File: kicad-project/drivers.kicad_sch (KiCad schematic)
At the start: 11 parts

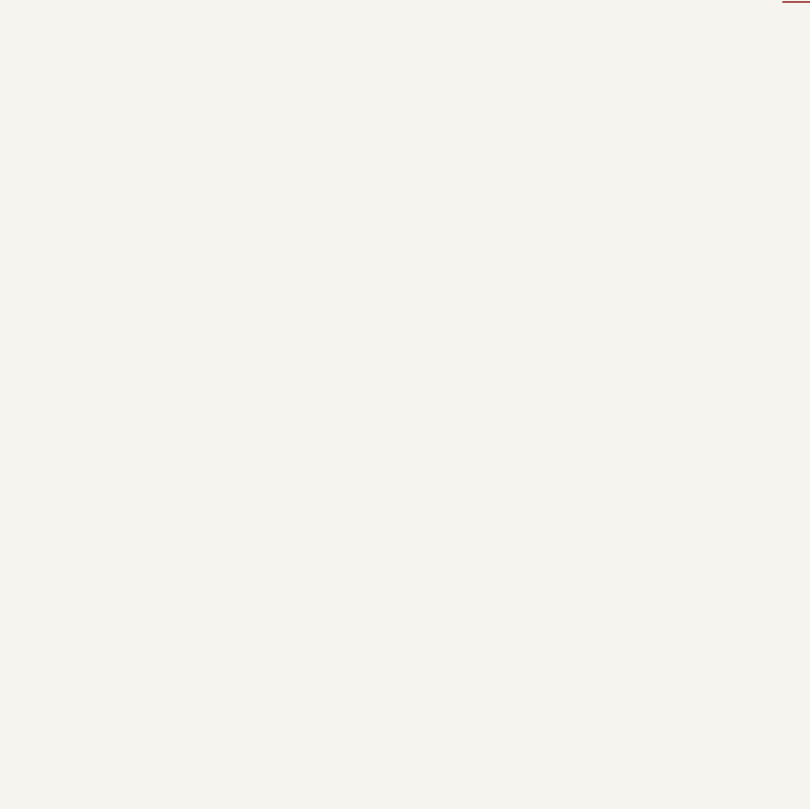
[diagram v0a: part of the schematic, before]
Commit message: hw: rename poject and create project library
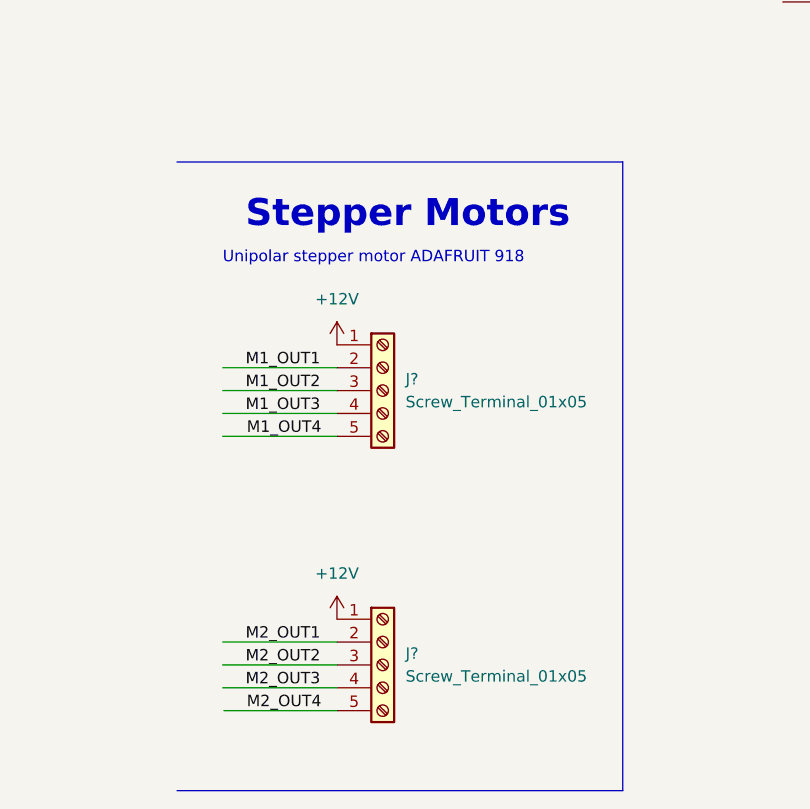
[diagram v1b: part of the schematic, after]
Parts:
- added J? (x2): Screw_Terminal_01x05, TerminalBlock_TE-Connectivity:TerminalBlock_TE_282834-5_1x05_P2.54mm_Horizontal, symbol Connector:Screw_Terminal_01x05
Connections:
- net +12V: now also J?.1 (Pin_1), J?.1 (Pin_1)
- new net M1_OUT1: J?.2 (Pin_2)
- new net M1_OUT2: J?.3 (Pin_3)
- new net M1_OUT3: J?.4 (Pin_4)
- new net M1_OUT4: J?.5 (Pin_5)
- new net M2_OUT1: J?.2 (Pin_2)
- new net M2_OUT2: J?.3 (Pin_3)
- new net M2_OUT3: J?.4 (Pin_4)
- new net M2_OUT4: J?.5 (Pin_5)
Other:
- note added: "Stepper Motors"
- note added: "Unipolar stepper motor ADAFRUIT 918"
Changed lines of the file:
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@@
+    (stroke (width 0) (type default) (color 0 0 0 0))
+  )
+  (wire (pts (xy 128.27 154.94) (xy 140.97 154.94))
     (stroke (width 0) (type default) (color 0 0 0 0))
   )
@@
     (stroke (width 0) (type default) (color 0 0 0 0))
   )
+  (wire (pts (xy 128.3981 185.42) (xy 140.97 185.42))
+    (stroke (width 0) (type default) (color 0 0 0 0))
+  )
   (wire (pts (xy 36.83 64.77) (xy 58.42 64.77))
     (stroke (width 0) (type default) (color 0 0 0 0))
@@
     (stroke (width 0) (type default) (color 0 0 0 0))
   )
+  (wire (pts (xy 128.27 177.8) (xy 140.97 177.8))
+    (stroke (width 0) (type default) (color 0 0 0 0))
+  )
+  (wire (pts (xy 128.27 149.86) (xy 140.97 149.86))
+    (stroke (width 0) (type default) (color 0 0 0 0))
+  )
   (wire (pts (xy 88.9 87.63) (xy 96.52 87.63))
     (stroke (width 0) (type default) (color 0 0 0 0))
@@
     (stroke (width 0) (type default) (color 0 0 0 0))
   )
+  (polyline (pts (xy 123.19 124.46) (xy 172.72 124.46))
+    (stroke (width 0) (type default) (color 0 0 0 0))
+  )
   (wire (pts (xy 110.49 50.8) (xy 123.19 50.8))
     (stroke (width 0) (type default) (color 0 0 0 0))
   )
+  (polyline (pts (xy 172.72 194.31) (xy 172.72 124.46))
+    (stroke (width 0) (type default) (color 0 0 0 0))
+  )
   (wire (pts (xy 97.79 30.48) (xy 109.22 30.48))
     (stroke (width 0) (type default) (color 0 0 0 0))
   )
+  (wire (pts (xy 128.27 180.34) (xy 140.97 180.34))
+    (stroke (width 0) (type default) (color 0 0 0 0))
+  )
   (wire (pts (xy 88.9 85.09) (xy 107.95 85.09))
     (stroke (width 0) (type default) (color 0 0 0 0))
@@
     (stroke (width 0) (type default) (color 0 0 0 0))
   )
+  (wire (pts (xy 128.27 147.32) (xy 140.97 147.32))
+    (stroke (width 0) (type default) (color 0 0 0 0))
+  )
+  (wire (pts (xy 128.27 182.88) (xy 140.97 182.88))
+    (stroke (width 0) (type default) (color 0 0 0 0))
+  )
   (wire (pts (xy 88.9 50.8) (xy 88.9 52.07))
     (stroke (width 0) (type default) (color 0 0 0 0))
@@
     (stroke (width 0) (type default) (color 0 0 0 0))
   )
+  (polyline (pts (xy 123.19 194.31) (xy 172.72 194.31))
+    (stroke (width 0) (type default) (color 0 0 0 0))
+  )
+  (wire (pts (xy 128.27 152.4) (xy 140.97 152.4))
+    (stroke (width 0) (type default) (color 0 0 0 0))
+  )
   (wire (pts (xy 97.79 59.69) (xy 97.79 60.96))
     (stroke (width 0) (type default) (color 0 0 0 0))
@@
     (stroke (width 0) (type default) (color 0 0 0 0))
   )
+  (text "Unipolar stepper motor ADAFRUIT 918" (at 128.27 135.89 0)
+    (effects (font (size 1.27 1.27)) (justify left bottom))
+  )
+  (text "Stepper Motors\n" (at 130.81 132.08 0)
+    (effects (font (size 3 3) (thickness 0.6) bold) (justify left bottom))
+  )
   (label "VBB" (at 91.44 50.8 0)
     (effects (font (size 1.27 1.27)) (justify left bottom))
   )
+  (label "M1_OUT3" (at 130.81 152.4 0)
+    (effects (font (size 1.27 1.27)) (justify left bottom))
+  )
   (label "VCP" (at 100.33 60.96 0)
+    (effects (font (size 1.27 1.27)) (justify left bottom))
+  )
+  (label "M2_OUT1" (at 130.81 177.8 0)
+    (effects (font (size 1.27 1.27)) (justify left bottom))
+  )
+  (label "M2_OUT3" (at 130.81 182.88 0)
+    (effects (font (size 1.27 1.27)) (justify left bottom))
+  )
+  (label "M2_OUT4" (at 130.9381 185.42 0)
     (effects (font (size 1.27 1.27)) (justify left bottom))
   )
@@
     (effects (font (size 1.27 1.27)) (justify left bottom))
   )
+  (label "M1_OUT4" (at 130.9381 154.94 0)
+    (effects (font (size 1.27 1.27)) (justify left bottom))
+  )
+  (label "M1_OUT2" (at 130.81 149.86 0)
+    (effects (font (size 1.27 1.27)) (justify left bottom))
+  )
   (label "SLEEP" (at 54.61 67.31 180)
     (effects (font (size 1.27 1.27)) (justify right bottom))
+  )
+  (label "M2_OUT2" (at 130.81 180.34 0)
+    (effects (font (size 1.27 1.27)) (justify left bottom))
+  )
+  (label "M1_OUT1" (at 130.81 147.32 0)
+    (effects (font (size 1.27 1.27)) (justify left bottom))
   )
   (symbol (lib_name "A4988SETTR-T_1") (lib_id "A4988:A4988SETTR-T") (at 210.82 81.28 0) (unit 1)
@@
     (pin "9")
   )
+  (symbol (lib_id "power:+12V") (at 140.97 175.26 0) (unit 1)
+    (in_bom yes) (on_board yes) (fields_autoplaced)
+    (property "Reference" "#PWR?" (id 0) (at 140.97 179.07 0)
+      (effects (font (size 1.27 1.27)) hide)
+    )
+    (property "Value" "+12V" (id 1) (at 140.97 170.18 0))
+    (property "Footprint" "" (id 2) (at 140.97 175.26 0)
+      (effects (font (size 1.27 1.27)) hide)
+    )
+    (property "Datasheet" "" (id 3) (at 140.97 175.26 0)
+      (effects (font (size 1.27 1.27)) hide)
+    )
+    (pin "1")
+  )
   (symbol (lib_id "power:GND") (at 107.95 92.71 0) (unit 1)
     (in_bom yes) (on_board yes) (fields_autoplaced)
@@
     (pin "9")
   )
+  (symbol (lib_id "Connector:Screw_Terminal_01x05") (at 146.05 180.34 0) (unit 1)
+    (in_bom yes) (on_board yes) (fields_autoplaced)
+    (property "Reference" "J?" (id 0) (at 148.59 179.0699 0)
+      (effects (font (size 1.27 1.27)) (justify left))
+    )
+    (property "Value" "Screw_Terminal_01x05" (id 1) (at 148.59 181.6099 0)
+      (effects (font (size 1.27 1.27)) (justify left))
+    )
+    (property "Footprint" "TerminalBlock_TE-Connectivity:TerminalBlock_TE_282834-5_1x05_P2.54mm_Horizontal" (id 2) (at 146.05 180.34 0)
+      (effects (font (size 1.27 1.27)) hide)
+    )
+    (property "Datasheet" "~" (id 3) (at 146.05 180.34 0)
+      (effects (font (size 1.27 1.27)) hide)
+    )
+    (pin "1")
+    (pin "2")
+    (pin "3")
+    (pin "4")
+    (pin "5")
+  )
   (symbol (lib_id "Device:C") (at 97.79 38.1 0) (unit 1)
     (in_bom yes) (on_board yes) (fields_autoplaced)
@@
     (pin "2")
   )
+  (symbol (lib_id "power:+12V") (at 140.97 144.78 0) (unit 1)
+    (in_bom yes) (on_board yes) (fields_autoplaced)
+    (property "Reference" "#PWR?" (id 0) (at 140.97 148.59 0)
+      (effects (font (size 1.27 1.27)) hide)
+    )
+    (property "Value" "+12V" (id 1) (at 140.97 139.7 0))
+    (property "Footprint" "" (id 2) (at 140.97 144.78 0)
+      (effects (font (size 1.27 1.27)) hide)
+    )
+    (property "Datasheet" "" (id 3) (at 140.97 144.78 0)
+      (effects (font (size 1.27 1.27)) hide)
+    )
+    (pin "1")
+  )
+  (symbol (lib_id "Connector:Screw_Terminal_01x05") (at 146.05 149.86 0) (unit 1)
+    (in_bom yes) (on_board yes) (fields_autoplaced)
+    (property "Reference" "J?" (id 0) (at 148.59 148.5899 0)
+      (effects (font (size 1.27 1.27)) (justify left))
+    )
+    (property "Value" "Screw_Terminal_01x05" (id 1) (at 148.59 151.1299 0)
+      (effects (font (size 1.27 1.27)) (justify left))
+    )
+    (property "Footprint" "TerminalBlock_TE-Connectivity:TerminalBlock_TE_282834-5_1x05_P2.54mm_Horizontal" (id 2) (at 146.05 149.86 0)
+      (effects (font (size 1.27 1.27)) hide)
+    )
+    (property "Datasheet" "~" (id 3) (at 146.05 149.86 0)
+      (effects (font (size 1.27 1.27)) hide)
+    )
+    (pin "1")
+    (pin "2")
+    (pin "3")
+    (pin "4")
+    (pin "5")
+  )
   (symbol (lib_id "power:GND") (at 88.9 102.87 0) (unit 1)

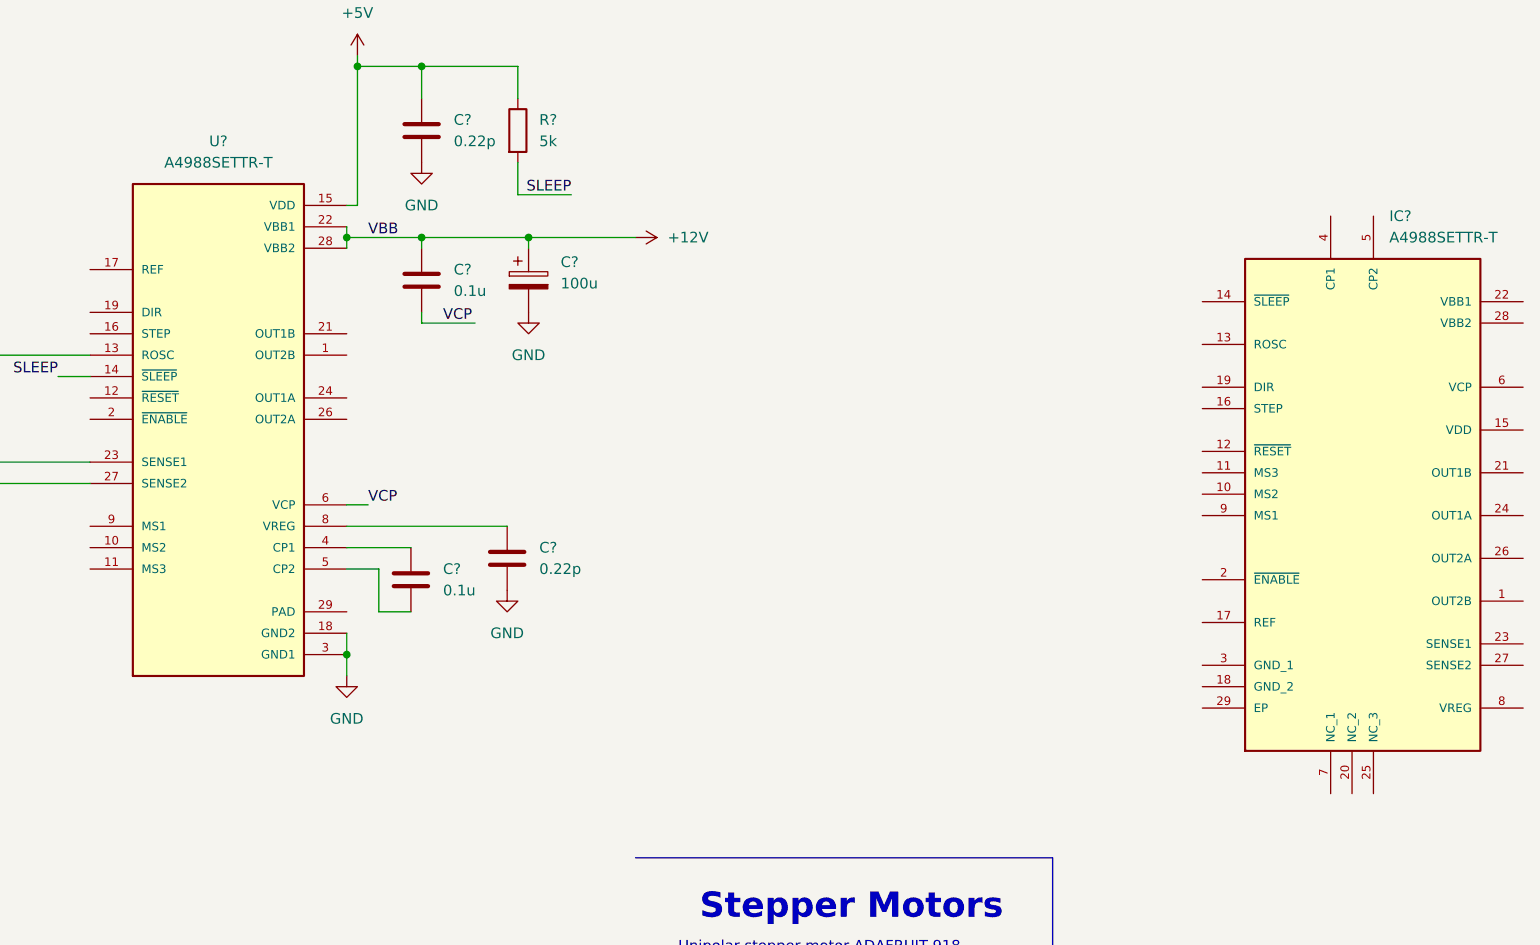
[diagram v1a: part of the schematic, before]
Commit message: hw: add power managment
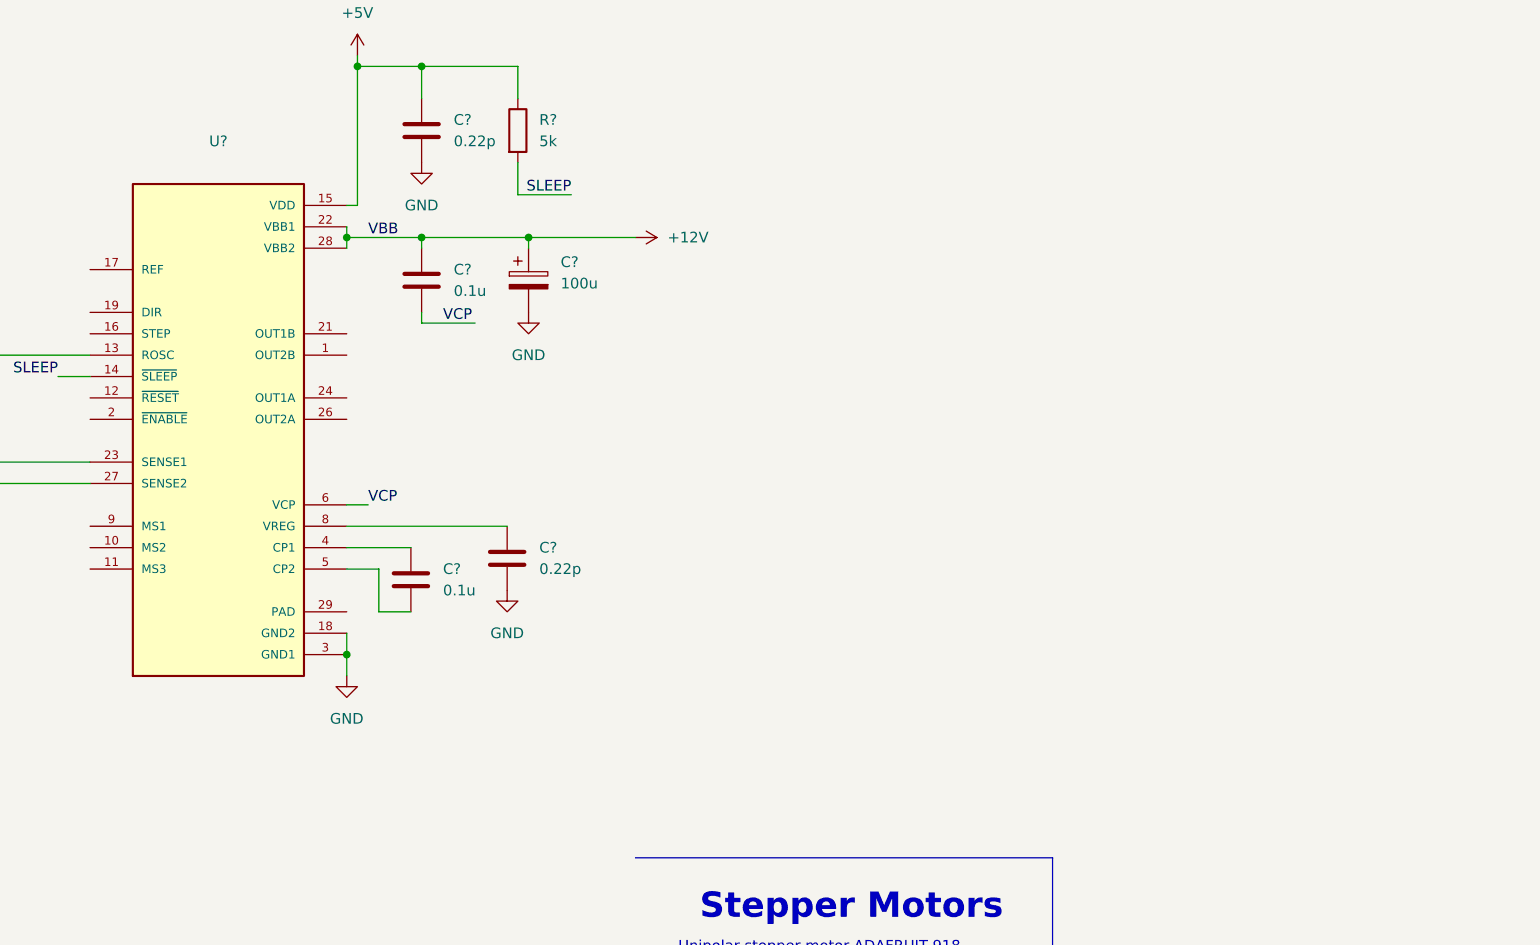
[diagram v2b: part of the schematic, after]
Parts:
- removed IC?: A4988SETTR-T, QFN50P500X500X100-29N, symbol A4988:A4988SETTR-T
- U?: value A4988SETTR-T -> (none); footprint QFN50P500X500X90-29N -> (none)
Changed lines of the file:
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@@
     (effects (font (size 1.27 1.27)) (justify left bottom))
-  )
-  (symbol (lib_name "A4988SETTR-T_1") (lib_id "A4988:A4988SETTR-T") (at 210.82 81.28 0) (unit 1)
-    (in_bom yes) (on_board yes) (fields_autoplaced)
-    (property "Reference" "IC?" (id 0) (at 212.6997 48.26 0)
-      (effects (font (size 1.27 1.27)) (justify left))
-    )
-    (property "Value" "A4988SETTR-T" (id 1) (at 212.6997 50.8 0)
-      (effects (font (size 1.27 1.27)) (justify left))
-    )
-    (property "Footprint" "QFN50P500X500X100-29N" (id 2) (at 210.82 81.28 0)
-      (effects (font (size 1.27 1.27)) (justify left bottom) hide)
-    )
-    (property "Datasheet" "" (id 3) (at 210.82 81.28 0)
-      (effects (font (size 1.27 1.27)) (justify left bottom) hide)
-    )
-    (property "RS_PART_NUMBER" "" (id 4) (at 210.82 81.28 0)
-      (effects (font (size 1.27 1.27)) (justify left bottom) hide)
-    )
-    (property "MOUSER_PRICE-STOCK" "" (id 5) (at 210.82 81.28 0)
-      (effects (font (size 1.27 1.27)) (justify left bottom) hide)
-    )
-    (property "MANUFACTURER_PART_NUMBER" "A4988SETTR-T" (id 6) (at 210.82 81.28 0)
-      (effects (font (size 1.27 1.27)) (justify left bottom) hide)
-    )
-    (property "MOUSER_PART_NUMBER" "" (id 7) (at 210.82 81.28 0)
-      (effects (font (size 1.27 1.27)) (justify left bottom) hide)
-    )
-    (property "DESCRIPTION" "DMOS Microstepping Driver with Translator  and Overcurrent Protection" (id 8) (at 210.82 81.28 0)
-      (effects (font (size 1.27 1.27)) (justify left bottom) hide)
-    )
-    (property "RS_PRICE-STOCK" "" (id 9) (at 210.82 81.28 0)
-      (effects (font (size 1.27 1.27)) (justify left bottom) hide)
-    )
-    (property "MANUFACTURER_NAME" "Allegro Microsystems" (id 10) (at 210.82 81.28 0)
-      (effects (font (size 1.27 1.27)) (justify left bottom) hide)
-    )
-    (property "HEIGHT" "1mm" (id 11) (at 210.82 81.28 0)
-      (effects (font (size 1.27 1.27)) (justify left bottom) hide)
-    )
-    (pin "1")
-    (pin "10")
-    (pin "11")
-    (pin "12")
-    (pin "13")
-    (pin "14")
-    (pin "15")
-    (pin "16")
-    (pin "17")
-    (pin "18")
-    (pin "19")
-    (pin "2")
-    (pin "20")
-    (pin "21")
-    (pin "22")
-    (pin "23")
-    (pin "24")
-    (pin "25")
-    (pin "26")
-    (pin "27")
-    (pin "28")
-    (pin "29")
-    (pin "3")
-    (pin "4")
-    (pin "5")
-    (pin "6")
-    (pin "7")
-    (pin "8")
-    (pin "9")
   )
   (symbol (lib_id "power:+12V") (at 140.97 175.26 0) (unit 1)
@@
     (in_bom yes) (on_board yes) (fields_autoplaced)
     (property "Reference" "U?" (id 0) (at 73.66 39.37 0))
-    (property "Value" "A4988SETTR-T" (id 1) (at 73.66 41.91 0))
-    (property "Footprint" "QFN50P500X500X90-29N" (id 2) (at 63.5 41.91 0)
+    (property "Value" "" (id 1) (at 73.66 41.91 0))
+    (property "Footprint" "" (id 2) (at 63.5 41.91 0)
       (effects (font (size 1.27 1.27)) (justify left bottom) hide)
     )

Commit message: hw: update
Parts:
- removed J?: Screw_Terminal_01x05, TerminalBlock_TE-Connectivity:TerminalBlock_TE_282834-5_1x05_P2.54mm_Horizontal, symbol Connector:Screw_Terminal_01x05
- removed R?: 5k, symbol Device:R
- C? (x2): value 0.22p -> (none)
- J?: value Screw_Terminal_01x05 -> (none); symbol Connector:Screw_Terminal_01x05 -> Connector:Screw_Terminal_01x04
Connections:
- net +12V: no longer C?.1, J?.1 (Pin_1)
- net +5V: now also U?.10 (MS2)
- net GND: now also U?.29 (PAD)
- net M1_OUT1: now also J?.1 (Pin_1), U?.21 (OUT1B); no longer J?.2 (Pin_2)
- net M1_OUT2: now also J?.2 (Pin_2), U?.1 (OUT2B); no longer J?.3 (Pin_3)
- net M1_OUT3: now also J?.3 (Pin_3), U?.24 (OUT1A); no longer J?.4 (Pin_4)
- net M1_OUT4: now also J?.4 (Pin_4), U?.26 (OUT2A); no longer J?.5 (Pin_5)
- net at U?.11 (MS3): now also U?.9 (MS1)
- net ~{HOME}: now reaches U?.12 (~{RESET})
- net M1_STEP: now reaches U?.16 (STEP)
- net M1_DIR: now reaches U?.19 (DIR)
- net ~{ENABLE}: now reaches U?.2 (~{ENABLE})
- net SLEEP: no longer names the net of U?.14 (~{SLEEP})
- no-connect marks 0 -> 1
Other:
- note added: "1/16 step"
- note added: "Bipolar M1"
- note added: "VREF, SENSE1 e 2 DA DIMENSIONARE"
- note removed: "Stepper Motors"
- note removed: "Unipolar stepper motor ADAFRUIT 918"
- moved on the sheet: C?, R?, U?
